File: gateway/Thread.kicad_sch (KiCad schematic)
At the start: 31 parts, among them IC1301 MIC5317-3.3xM5, IC1302 74LVC1G07, IC1303 TXB0104PWR, M1301 BT40, X1301 DEBUG

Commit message: Add INA219 for current measurement
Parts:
- renumbered R1308 to R1304, R1309 to R1305, R1310 to R1306, R1311 to R1307, R1304 to R1308, R1305 to R1309, R1306 to R1310, R1307 to R1311
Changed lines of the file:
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@@
 	(title_block
 		(title "Thread Router")
-		(date "2025-06-05")
+		(date "2026-07-09")
 		(rev "${REVISION}")
 		(company "${COMPANY}")
@@
 		(in_pos_files yes)
 		(dnp no)
-		(property "Reference" "R1310"
+		(property "Reference" "R1306"
 			(at 205.74 92.202 90)
 			(show_name no)
@@
 			(project "Gateway"
 				(path "/d5742f03-3b1a-42e5-a384-018bd4b919aa/c5103ceb-5325-4a84-a025-9638a412984e/38da7bfd-61a1-4734-9412-ab3ae9cd3f77"
-					(reference "R1310")
+					(reference "R1306")
 					(unit 1)
 				)
@@
 		(in_pos_files yes)
 		(dnp no)
-		(property "Reference" "R1305"
+		(property "Reference" "R1309"
 			(at 241.3 116.586 90)
 			(show_name no)
@@
 			(project "Gateway"
 				(path "/d5742f03-3b1a-42e5-a384-018bd4b919aa/c5103ceb-5325-4a84-a025-9638a412984e/38da7bfd-61a1-4734-9412-ab3ae9cd3f77"
-					(reference "R1305")
+					(reference "R1309")
 					(unit 1)
 				)
@@
 		(in_pos_files yes)
 		(dnp no)
-		(property "Reference" "R1307"
+		(property "Reference" "R1311"
 			(at 252.73 106.68 90)
 			(show_name no)
@@
 			(project "Gateway"
 				(path "/d5742f03-3b1a-42e5-a384-018bd4b919aa/c5103ceb-5325-4a84-a025-9638a412984e/38da7bfd-61a1-4734-9412-ab3ae9cd3f77"
-					(reference "R1307")
+					(reference "R1311")
 					(unit 1)
 				)
@@
 		(in_pos_files yes)
 		(dnp no)
-		(property "Reference" "R1309"
+		(property "Reference" "R1305"
 			(at 194.31 116.586 90)
 			(show_name no)
@@
 			(project "Gateway"
 				(path "/d5742f03-3b1a-42e5-a384-018bd4b919aa/c5103ceb-5325-4a84-a025-9638a412984e/38da7bfd-61a1-4734-9412-ab3ae9cd3f77"
-					(reference "R1309")
+					(reference "R1305")
 					(unit 1)
 				)
@@
 		(dnp no)
 		(fields_autoplaced yes)
-		(property "Reference" "R1304"
+		(property "Reference" "R1308"
 			(at 241.3 101.6 90)
 			(show_name no)
@@
 			(project "Gateway"
 				(path "/d5742f03-3b1a-42e5-a384-018bd4b919aa/c5103ceb-5325-4a84-a025-9638a412984e/38da7bfd-61a1-4734-9412-ab3ae9cd3f77"
-					(reference "R1304")
+					(reference "R1308")
 					(unit 1)
 				)
@@
 		(in_pos_files yes)
 		(dnp no)
-		(property "Reference" "R1306"
+		(property "Reference" "R1310"
 			(at 252.73 92.202 90)
 			(show_name no)
@@
 			(project "Gateway"
 				(path "/d5742f03-3b1a-42e5-a384-018bd4b919aa/c5103ceb-5325-4a84-a025-9638a412984e/38da7bfd-61a1-4734-9412-ab3ae9cd3f77"
-					(reference "R1306")
+					(reference "R1310")
 					(unit 1)
 				)
@@
 		(dnp no)
 		(fields_autoplaced yes)
-		(property "Reference" "R1308"
+		(property "Reference" "R1304"
 			(at 194.31 101.6 90)
 			(show_name no)
@@
 			(project "Gateway"
 				(path "/d5742f03-3b1a-42e5-a384-018bd4b919aa/c5103ceb-5325-4a84-a025-9638a412984e/38da7bfd-61a1-4734-9412-ab3ae9cd3f77"
-					(reference "R1308")
+					(reference "R1304")
 					(unit 1)
 				)
@@
 		(in_pos_files yes)
 		(dnp no)
-		(property "Reference" "R1311"
+		(property "Reference" "R1307"
 			(at 205.74 106.68 90)
 			(show_name no)
@@
 			(project "Gateway"
 				(path "/d5742f03-3b1a-42e5-a384-018bd4b919aa/c5103ceb-5325-4a84-a025-9638a412984e/38da7bfd-61a1-4734-9412-ab3ae9cd3f77"
-					(reference "R1311")
+					(reference "R1307")
 					(unit 1)
 				)

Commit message: Push outputs from CI/CD (2026-07-09 20:18:55)
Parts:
- added X1302: UART, Connector_PinHeader_2.54mm:PinHeader_1x03_P2.54mm_Vertical, symbol Connector_Generic:Conn_01x03
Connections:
- net GND: now also X1302.2 (Pin_2)
- net Thread-CTS: now also M1301.C4 (P0.23), R1304.1, TP1306.1; no longer M1301.C2 (P0.21), R1307.2, TP1305.1
- net Thread-RTS: now also M1301.C3 (P0.24), R1305.1, TP1308.1; no longer M1301.B1 (P0.19), R1306.1, TP1307.1
- net Thread-RxD: now also R1307.2, TP1305.1; no longer R1305.1, TP1308.1
- net Thread-TxD: now also R1306.1, TP1307.1; no longer R1304.1, TP1306.1
- net Thread.CTS: now also R1309.2; no longer R1310.2
- net Thread.RTS: now also R1308.2; no longer R1311.1
- net Thread.RxD: now also R1310.2; no longer R1308.2
- net Thread.TxD: now also R1311.1; no longer R1309.2
- net Console-TxD: now reaches M1301.1 (P1.02)
- net Console-TxD: now also X1302.1 (Pin_1)
- net Console-RxD: now reaches M1301.2 (P1.03)
- net Console-RxD: now also X1302.3 (Pin_3)
- no-connect marks 50 -> 48
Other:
- moved on the sheet: C1303, C1304, IC1303, R1304, R1305, R1306, R1307, R1308, R1309, R1310, R1311, TP1305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

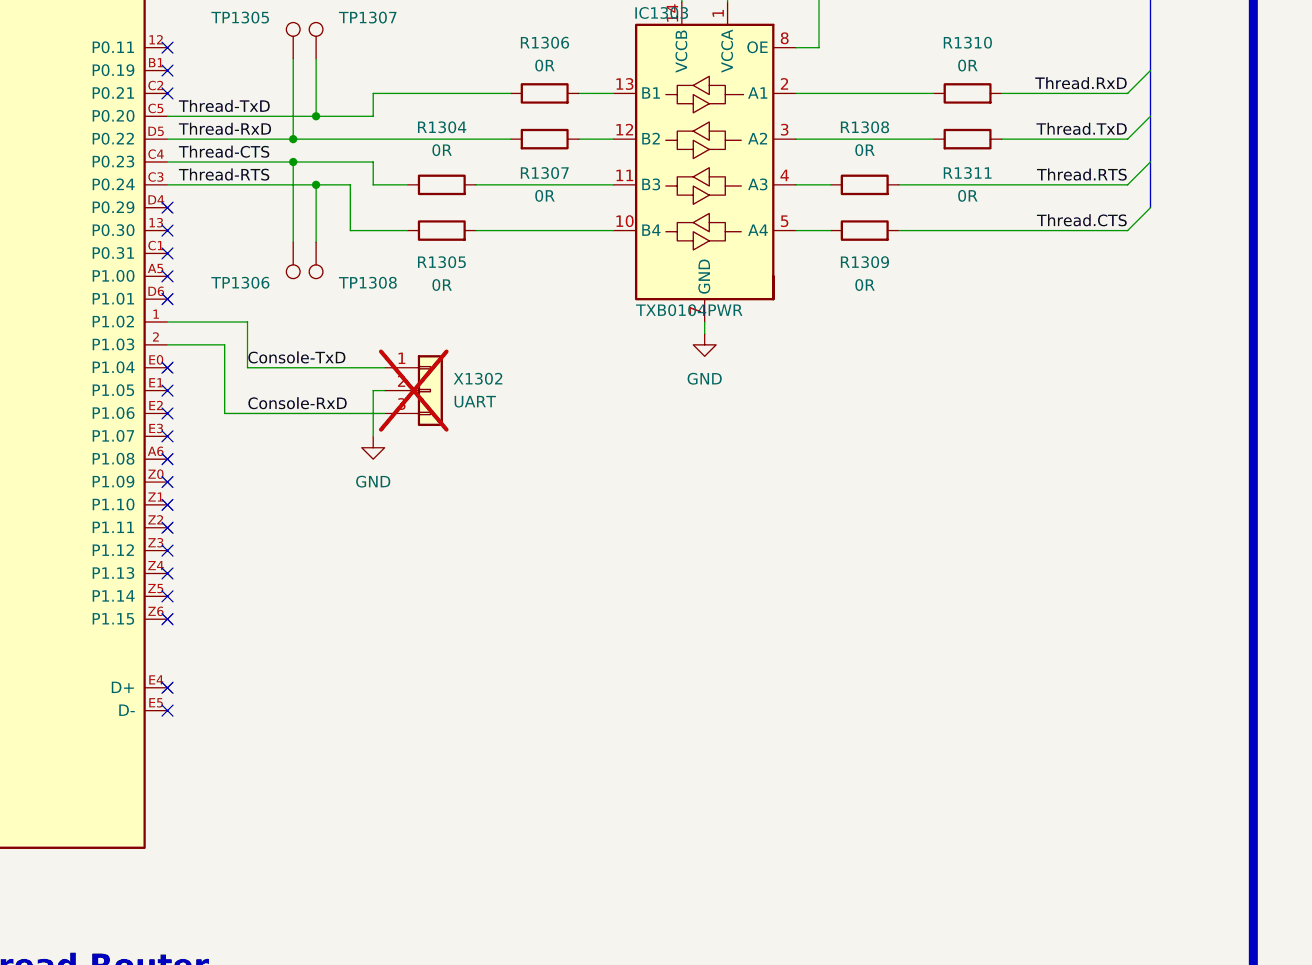
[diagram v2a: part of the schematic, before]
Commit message: Add boot signal for Thread MCU
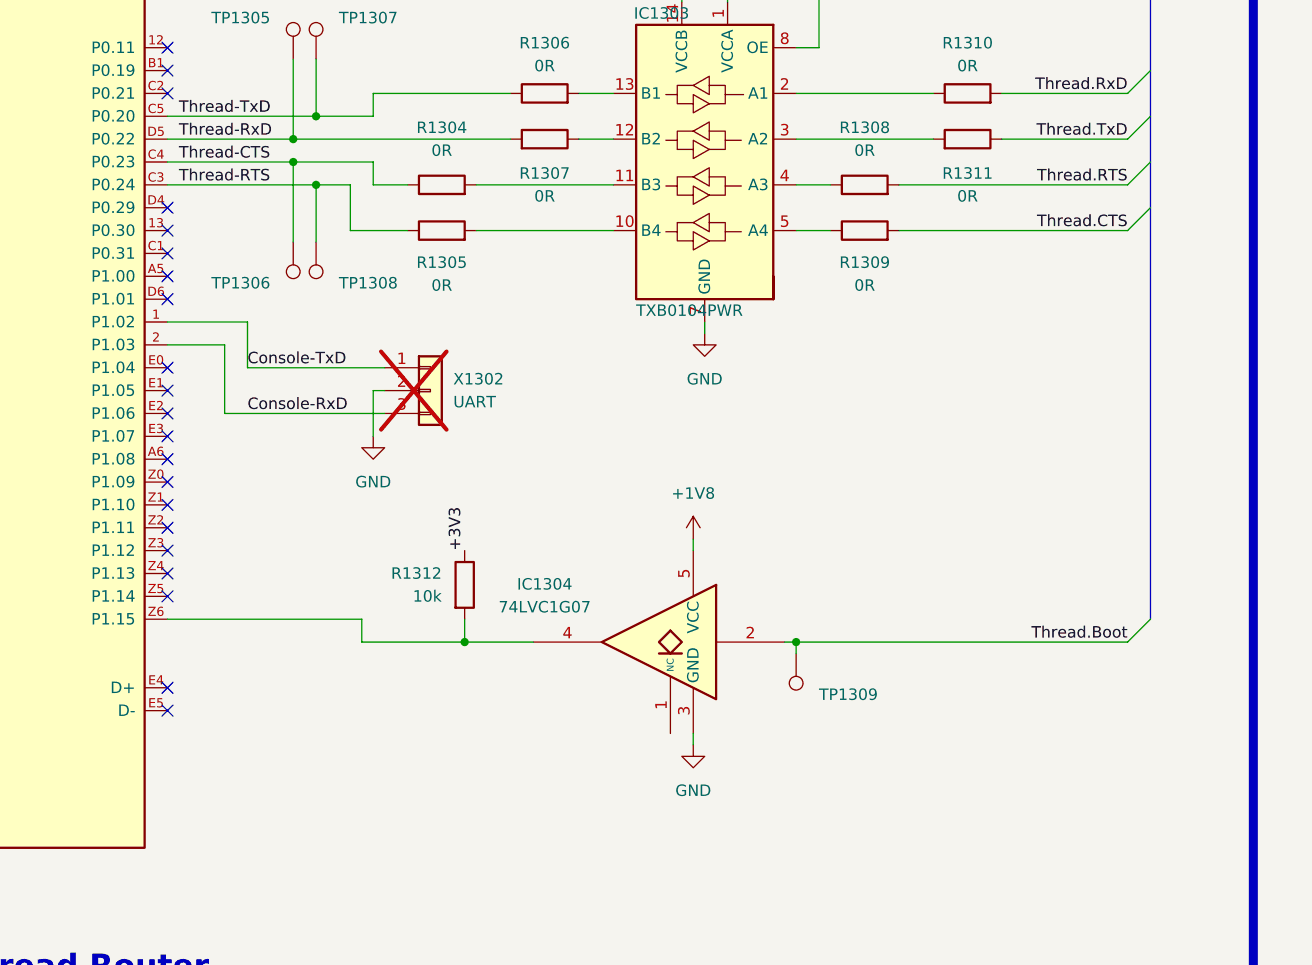
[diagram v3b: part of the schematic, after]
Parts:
- added IC1304: 74LVC1G07, Package_TO_SOT_SMD:SOT-353_SC-70-5, symbol 74xGxx:74LVC1G07
- added R1312: 10k, Resistor_SMD:R_0805_2012Metric, symbol Device:R
- added TP1309: ~, Testpoints_Kampi:TestPoint_Pad_1.0x1.0mm, symbol Connector:TestPoint
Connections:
- net +1V8: now also IC1304.5 (VCC)
- net +3V3: now also R1312.1
- net GND: now also IC1304.3 (GND)
- net at M1301.Z6 (P1.15): now also IC1304.4, R1312.2
- new net Thread.Boot: IC1304.2, TP1309.1
- no-connect marks 48 -> 47

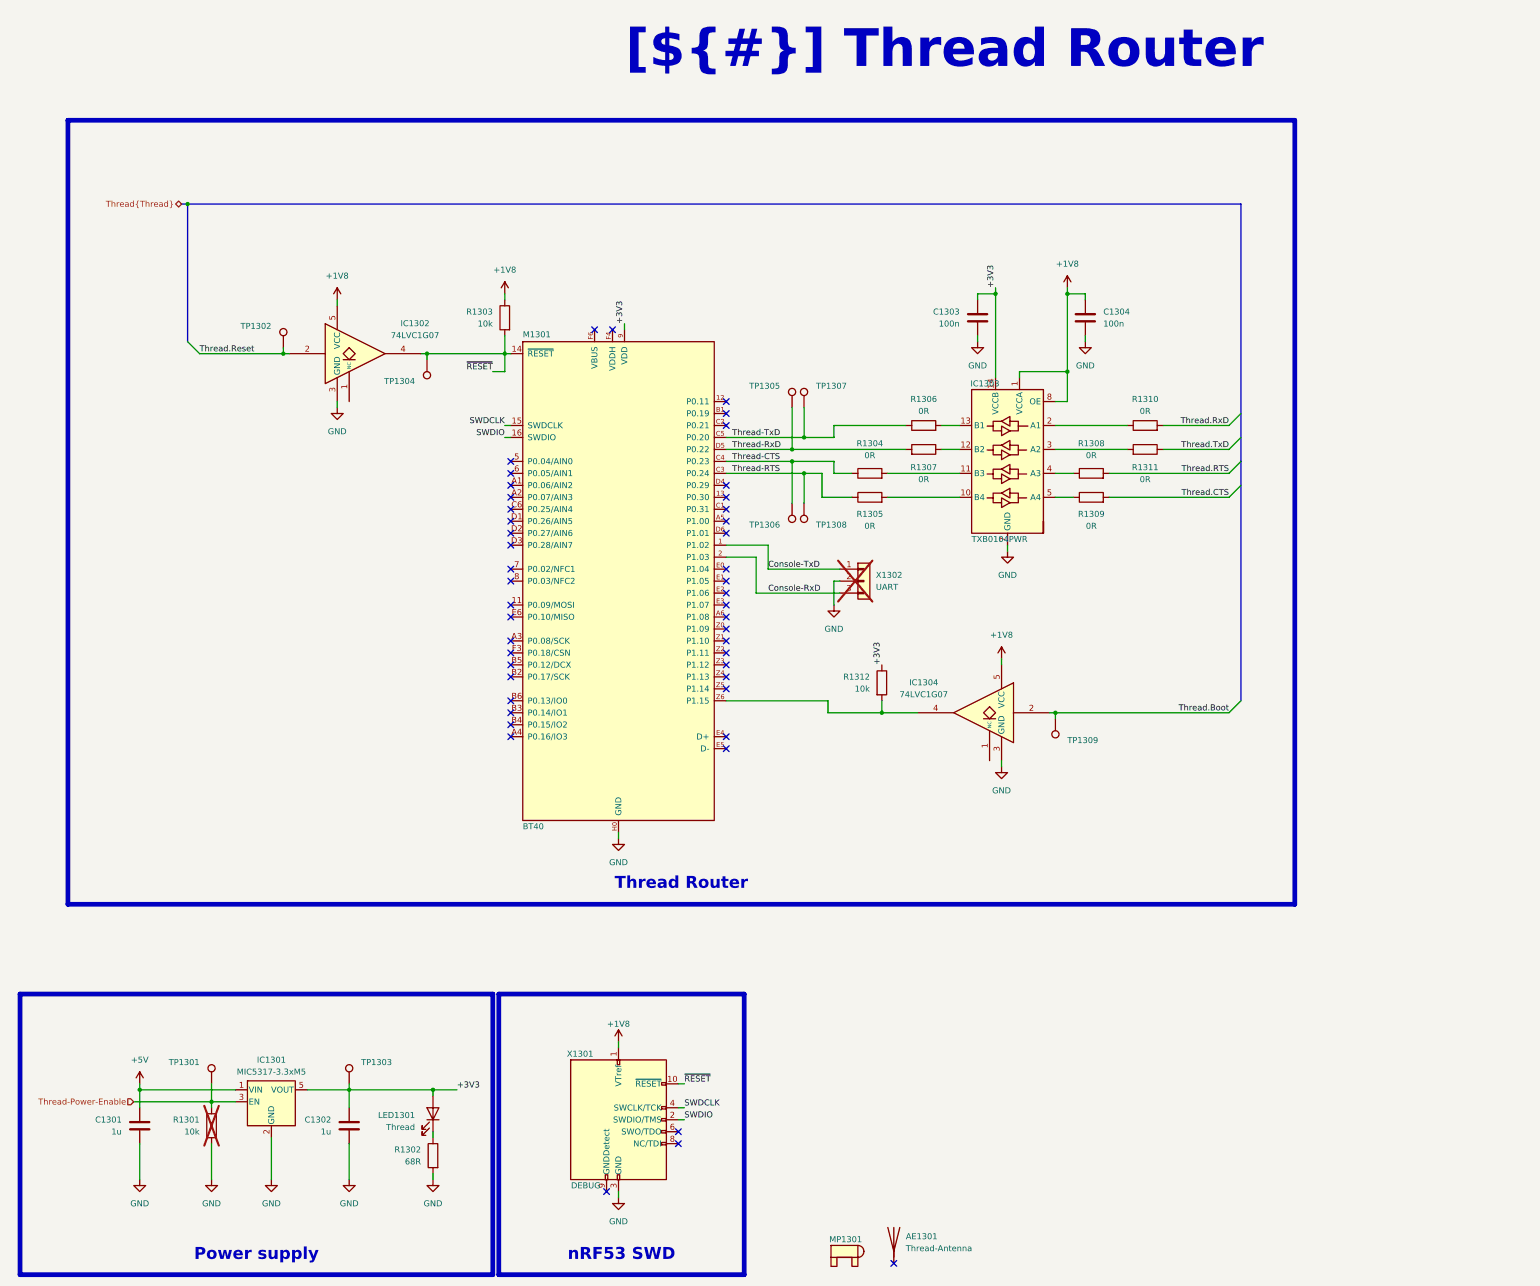
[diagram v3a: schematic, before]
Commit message: Improving Thread
- Add boot signal for Thread MCU
- Add debug LED for nRF5340
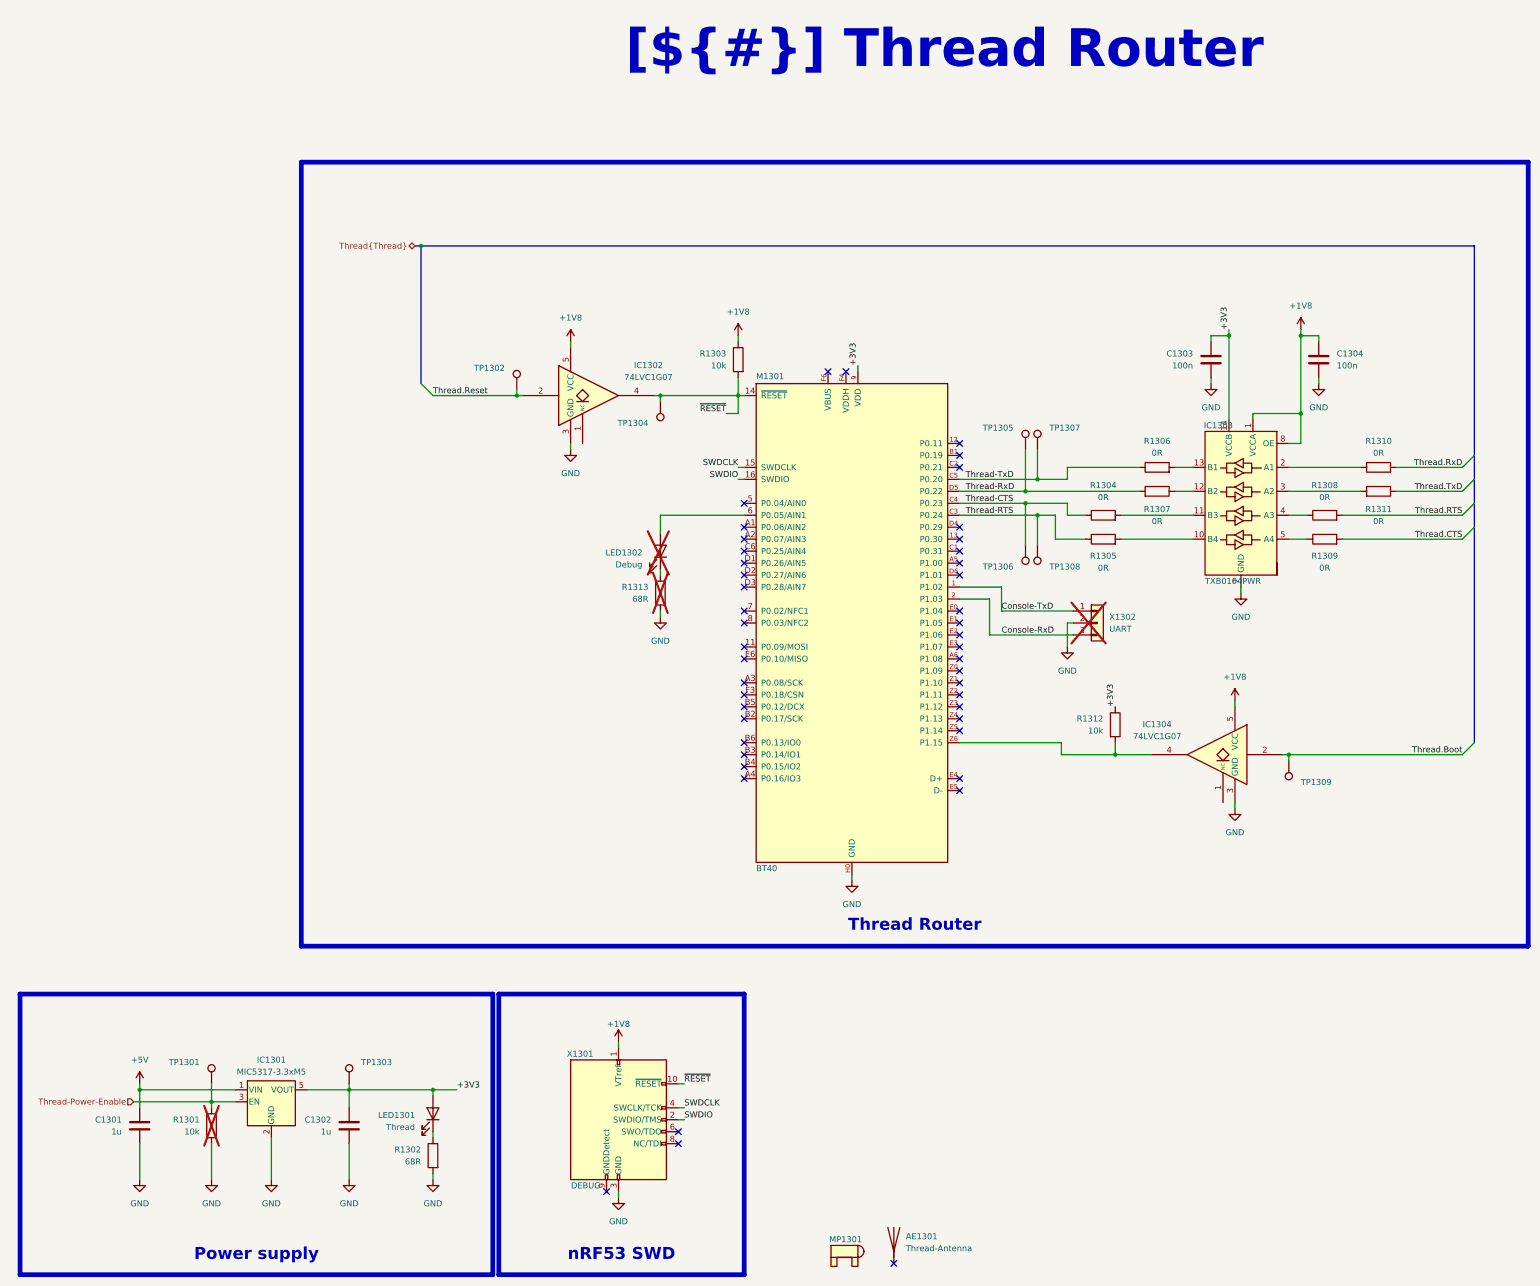
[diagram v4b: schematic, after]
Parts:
- added LED1302: Debug, LED_SMD:LED_0805_2012Metric, symbol Device:LED
- added R1313: 68R, Resistor_SMD:R_0805_2012Metric, symbol Device:R
- R1303: mouser# 652-CR0402-JW-103GLF -> 652-CR0805-JW-103GLF
- TP1301, TP1302, TP1303, TP1304, TP1305, TP1306, TP1307, TP1308, TP1309: value ~ -> (none)
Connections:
- net GND: now also R1313.2
- net at M1301.6 (P0.05/AIN1): now also LED1302.2 (A)
- new net: LED1302.1 (K), R1313.1
- no-connect marks 47 -> 46
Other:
- moved on the sheet: C1303, C1304, IC1302, IC1303, IC1304, M1301, R1303, R1304, R1305, R1306, R1307, R1308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

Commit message: Working on PCB
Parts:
- removed IC1301: MIC5317-3.3xM5, Package_TO_SOT_SMD:SOT-23-5, symbol Regulator_Linear:MIC5317-3.3xM5
- removed TP1305, TP1306, TP1307, TP1308: (no value), Testpoints_Kampi:TestPoint_Pad_1.0x1.0mm, symbol Connector:TestPoint
- added IC1301: TLV75733PDBV, Package_TO_SOT_SMD:SOT-23-5, symbol Regulator_Linear:TLV75733PDBV
- TP1301, TP1304, TP1309: value (none) -> ~
- TP1302: renamed from TP1303; value (none) -> ~
- TP1303: renamed from TP1302; value (none) -> ~
- renumbered IC1304 to IC1303, IC1303 to IC1304, R1313 to R1303, R1303 to R1304, R1304 to R1305, R1305 to R1306, R1312 to R1307, R1306 to R1308, R1307 to R1309, R1308 to R1310, R1309 to R1311, R1310 to R1312, R1311 to R1313
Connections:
- net +3V3: now also IC1301.5 (OUT)
- net +5V: now also IC1301.1 (IN)
- net GND: now also LED1302.1 (K), IC1301.2 (GND); no longer R1303.2
- net Thread-Power-Enable: now also IC1301.3 (EN)
- net at R1303.1: now also M1301.6 (P0.05/AIN1); no longer LED1302.1 (K)
- net at LED1302.2 (A): now also R1303.2; no longer M1301.6 (P0.05/AIN1)
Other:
- moved on the sheet: LED1302, R1303
